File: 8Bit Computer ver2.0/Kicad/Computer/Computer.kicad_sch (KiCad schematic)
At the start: 209 parts, among them IC1 MP2338GTL-Z, IC2 MP2338GTL-Z, IC266 SN74LVC1GU04DCKR, IC267 TMUX1309DYYR, IC268 SN74LVC1G14DBVR, IC269 LM555CMX_NOPB, IC270 SN74AHC74DR, IC274 SN74AHC540DWR, IC275 SN74AHC540DWR, IC276 SN74AHC540DWR, IC277 SN74AHC540DWR, IC278 SN74AHC540DWR, IC279 SN74AHC540DWR, IC3 DS1100Z-150+, J1 M20-7910842R, J10 M20-7910842R, J11 M20-7910842R, J12 M20-7910842R, J13 M20-7910842R, J14 M20-7910842R, J15 M20-7910842R, J16 M20-7910842R, J17 M20-7910842R, J18 M20-8890845, J19 M20-8890845, J2 M20-7910842R, J20 M20-8890845, J21 M20-8890845, J22 M20-8890845, J23 M20-8890845, J24 M20-8890845, J25 M20-8890845, J26 M20-8890845, J27 M20-8890845, J28 M20-8890845, J29 M20-8890845, J3 M20-7910842R, J30 M20-8890845, J31 M20-8890845, J32 M20-8890845, J33 M20-8890845, J34 M20-8890845, J38 M20-7910842R, J39 M20-7910842R, J4 M20-7910842R, J40 M20-7911042R, J41 M20-7911042R, J5 M20-7910842R, J6 M20-7910842R, J7 M20-7910842R, J8 M20-7910842R, J9 M20-7910842R, Y1 8MHz

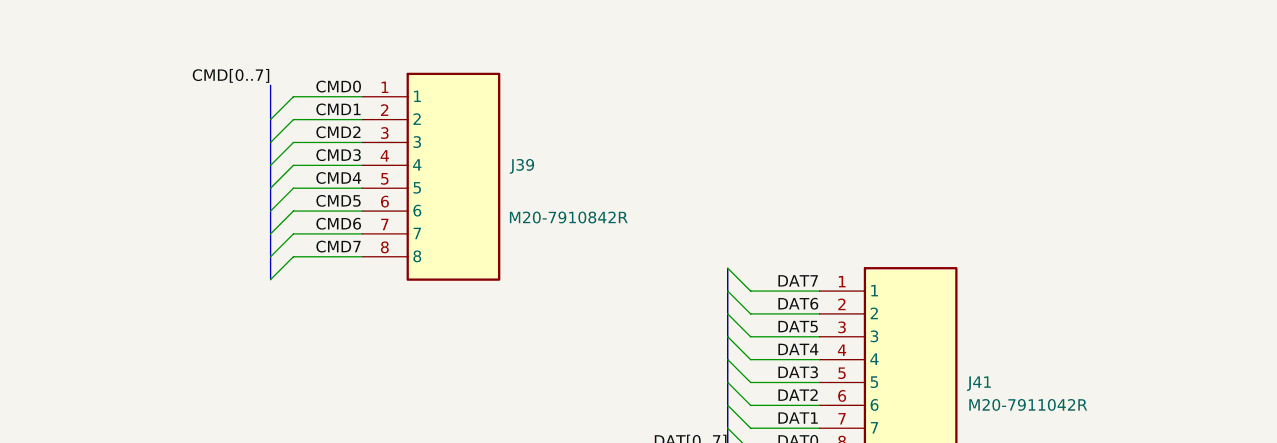
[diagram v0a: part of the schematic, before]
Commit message: Kicad
added Leds for B Bus and A Bus
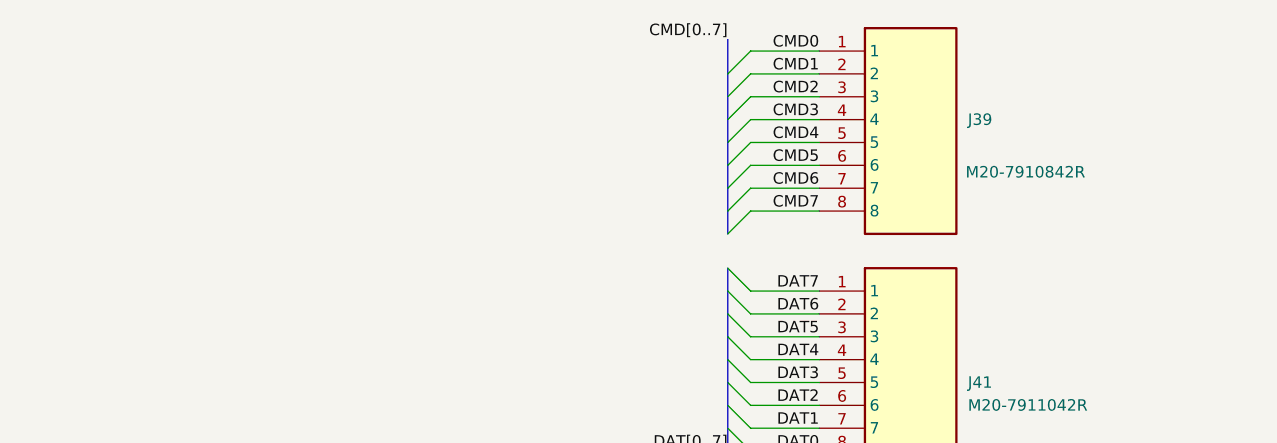
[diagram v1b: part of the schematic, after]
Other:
- moved on the sheet: J39
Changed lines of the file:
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@@
 	)
 	(bus_entry
-		(at 166.37 196.85)
+		(at 217.17 191.77)
 		(size 2.54 -2.54)
 		(stroke
@@
 	)
 	(bus_entry
-		(at 166.37 199.39)
+		(at 217.17 194.31)
 		(size 2.54 -2.54)
 		(stroke
@@
 	)
 	(bus_entry
-		(at 166.37 204.47)
+		(at 217.17 199.39)
 		(size 2.54 -2.54)
 		(stroke
@@
 	)
 	(bus_entry
-		(at 166.37 207.01)
+		(at 217.17 201.93)
 		(size 2.54 -2.54)
 		(stroke
@@
 	)
 	(bus_entry
-		(at 166.37 212.09)
+		(at 217.17 207.01)
 		(size 2.54 -2.54)
 		(stroke
@@
 	)
 	(bus_entry
-		(at 166.37 214.63)
+		(at 217.17 209.55)
 		(size 2.54 -2.54)
 		(stroke
@@
 	)
 	(bus_entry
-		(at 166.37 201.93)
+		(at 217.17 196.85)
 		(size 2.54 -2.54)
 		(stroke
@@
 	)
 	(bus_entry
-		(at 166.37 209.55)
+		(at 217.17 204.47)
 		(size 2.54 -2.54)
 		(stroke
@@
 	(bus
 		(pts
-			(xy 166.37 207.01) (xy 166.37 209.55)
+			(xy 217.17 201.93) (xy 217.17 204.47)
 		)
 		(stroke
@@
 	(bus
 		(pts
-			(xy 166.37 196.85) (xy 166.37 199.39)
+			(xy 217.17 191.77) (xy 217.17 194.31)
 		)
 		(stroke
@@
 	(wire
 		(pts
-			(xy 176.53 196.85) (xy 168.91 196.85)
+			(xy 227.33 191.77) (xy 219.71 191.77)
 		)
 		(stroke
@@
 	(bus
 		(pts
-			(xy 166.37 204.47) (xy 166.37 207.01)
+			(xy 217.17 199.39) (xy 217.17 201.93)
 		)
 		(stroke
@@
 	(bus
 		(pts
-			(xy 166.37 193.04) (xy 166.37 196.85)
+			(xy 217.17 187.96) (xy 217.17 191.77)
 		)
 		(stroke
@@
 	(wire
 		(pts
-			(xy 176.53 199.39) (xy 168.91 199.39)
+			(xy 227.33 194.31) (xy 219.71 194.31)
 		)
 		(stroke
@@
 	(bus
 		(pts
-			(xy 166.37 212.09) (xy 166.37 214.63)
+			(xy 217.17 207.01) (xy 217.17 209.55)
 		)
 		(stroke
@@
 	(wire
 		(pts
-			(xy 176.53 201.93) (xy 168.91 201.93)
+			(xy 227.33 196.85) (xy 219.71 196.85)
 		)
 		(stroke
@@
 	(wire
 		(pts
-			(xy 176.53 194.31) (xy 168.91 194.31)
+			(xy 227.33 189.23) (xy 219.71 189.23)
 		)
 		(stroke
@@
 	(bus
 		(pts
-			(xy 166.37 199.39) (xy 166.37 201.93)
+			(xy 217.17 194.31) (xy 217.17 196.85)
 		)
 		(stroke
@@
 	(wire
 		(pts
-			(xy 176.53 204.47) (xy 168.91 204.47)
+			(xy 227.33 199.39) (xy 219.71 199.39)
 		)
 		(stroke
@@
 	(bus
 		(pts
-			(xy 166.37 201.93) (xy 166.37 204.47)
+			(xy 217.17 196.85) (xy 217.17 199.39)
 		)
 		(stroke
@@
 	(wire
 		(pts
-			(xy 176.53 207.01) (xy 168.91 207.01)
+			(xy 227.33 201.93) (xy 219.71 201.93)
 		)
 		(stroke
@@
 	(wire
 		(pts
-			(xy 176.53 212.09) (xy 168.91 212.09)
+			(xy 227.33 207.01) (xy 219.71 207.01)
 		)
 		(stroke
@@
 	(wire
 		(pts
-			(xy 176.53 209.55) (xy 168.91 209.55)
+			(xy 227.33 204.47) (xy 219.71 204.47)
 		)
 		(stroke
@@
 	(bus
 		(pts
-			(xy 166.37 209.55) (xy 166.37 212.09)
+			(xy 217.17 204.47) (xy 217.17 207.01)
 		)
 		(stroke
@@
 	)
 	(label "CMD6"
-		(at 176.53 209.55 180)
+		(at 227.33 204.47 180)
 		(effects
 			(font
@@
 	)
 	(label "CMD3"
-		(at 176.53 201.93 180)
+		(at 227.33 196.85 180)
 		(effects
 			(font
@@
 	)
 	(label "CMD5"
-		(at 176.53 207.01 180)
+		(at 227.33 201.93 180)
 		(effects
 			(font
@@
 	)
 	(label "CMD2"
-		(at 176.53 199.39 180)
+		(at 227.33 194.31 180)
 		(effects
 			(font
@@
 	)
 	(label "CMD4"
-		(at 176.53 204.47 180)
+		(at 227.33 199.39 180)
 		(effects
 			(font
@@
 	)
 	(label "CMD7"
-		(at 176.53 212.09 180)
+		(at 227.33 207.01 180)
 		(effects
 			(font
@@
 	)
 	(label "CMD[0..7]"
-		(at 166.37 193.04 180)
+		(at 217.17 187.96 180)
 		(effects
 			(font
@@
 	)
 	(label "CMD0"
-		(at 176.53 194.31 180)
+		(at 227.33 189.23 180)
 		(effects
 			(font
@@
 	)
 	(label "CMD1"
-		(at 176.53 196.85 180)
+		(at 227.33 191.77 180)
 		(effects
 			(font
@@
 	(symbol
 		(lib_id "Samacsys:M20-7910842R")
-		(at 176.53 194.31 0)
+		(at 227.33 189.23 0)
 		(unit 1)
 		(exclude_from_sim no)
@@
 		(dnp no)
 		(property "Reference" "J39"
-			(at 193.04 201.9299 0)
+			(at 243.84 196.8499 0)
 			(effects
 				(font
@@
 		)
 		(property "Value" "M20-7910842R"
-			(at 192.786 207.772 0)
+			(at 243.586 202.692 0)
 			(effects
 				(font
@@
 		)
 		(property "Footprint" "Samacsys:M207910842R"
-			(at 193.04 289.23 0)
+			(at 243.84 284.15 0)
 			(effects
 				(font
@@
 		)
 		(property "Datasheet" "https://www.digikey.ph/en/products/detail/harwin-inc/M20-7910842R/6559285?msockid=39f1ec84d77b6f4428b7f904d6676eed"
-			(at 193.04 389.23 0)
+			(at 243.84 384.15 0)
 			(effects
 				(font
@@
 		)
 		(property "Description" "2.54mm (0.1\") Pitch SIL Horizontal SMT Socket Assembly, selective gold + tin (Tape & Reel packing), 8 contacts"
-			(at 176.53 194.31 0)
+			(at 227.33 189.23 0)
 			(effects
 				(font
@@
 		)
 		(property "Height" "2.65"
-			(at 193.04 589.23 0)
+			(at 243.84 584.15 0)
 			(effects
 				(font
@@
 		)
 		(property "Mouser Part Number" "855-M20-7910842R"
-			(at 193.04 689.23 0)
+			(at 243.84 684.15 0)
 			(effects
 				(font
@@
 		)
 		(property "Mouser Price/Stock" "https://www.mouser.co.uk/ProductDetail/Harwin/M20-7910842R?qs=k41KVqW3ympJ6ZCQNkwKKw%3D%3D"
-			(at 193.04 789.23 0)
+			(at 243.84 784.15 0)
 			(effects
 				(font
@@
 		)
 		(property "Manufacturer_Name" "Harwin"
-			(at 193.04 889.23 0)
+			(at 243.84 884.15 0)
 			(effects
 				(font
@@
 		)
 		(property "Manufacturer_Part_Number" "M20-7910842R"
-			(at 193.04 989.23 0)
+			(at 243.84 984.15 0)
 			(effects
 				(font

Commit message: Kicad Fixes only schematic
fixed important schematic errors
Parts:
- R112, R113, R114, R115, R116, R117, R118, R119, R120, R121, R122, R123, R124, R125, R126, R127, R128, R129, R130, R131, R132, R133, R134, R135, R136, R137, R138, R139, R140, R141, R142, R143, R144, R145, R146, R147, R148, R149, R150, R151, R152, R153, R154, R155, R156, R157, R158, R159: value 150 -> 390
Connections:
- net ADRM0: now also J27.1; no longer J27.8
- net ADRM1: now also J27.2; no longer J27.7
- net ADRM10: now also J28.3; no longer J28.6
- net ADRM11: now also J28.4; no longer J28.5
- net ADRM12: now also J28.5; no longer J28.4
- net ADRM13: now also J28.6; no longer J28.3
- net ADRM14: now also J28.7; no longer J28.2
- net ADRM15: now also J28.8; no longer J28.1
- net ADRM2: now also J27.3; no longer J27.6
- net ADRM3: now also J27.4; no longer J27.5
- net ADRM4: now also J27.5; no longer J27.4
- net ADRM5: now also J27.6; no longer J27.3
- net ADRM6: now also J27.7; no longer J27.2
- net ADRM7: now also J27.8; no longer J27.1
- net ADRM8: now also J28.1; no longer J28.8
- net ADRM9: now also J28.2; no longer J28.7
- net CMDM0: now also J29.1; no longer J29.8
- net CMDM1: now also J29.2; no longer J29.7
- net CMDM2: now also J29.3; no longer J29.6
- net CMDM3: now also J29.4; no longer J29.5
- net CMDM4: now also J29.5; no longer J29.4
- net CMDM5: now also J29.6; no longer J29.3
- net CMDM6: now also J29.7; no longer J29.2
- net CMDM7: now also J29.8; no longer J29.1
- net DATIO0: now also J33.1; no longer J33.8
- net DATIO1: now also J33.2; no longer J33.7
- net DATIO2: now also J33.3; no longer J33.6
- net DATIO3: now also J33.4; no longer J33.5
- net DATIO4: now also J33.5; no longer J33.4
- net DATIO5: now also J33.6; no longer J33.3
- net DATIO6: now also J33.7; no longer J33.2
- net DATIO7: now also J33.8; no longer J33.1
- net DATM0: now also J30.1; no longer J30.8
- net DATM1: now also J30.2; no longer J30.7
- net DATM2: now also J30.3; no longer J30.6
- net DATM3: now also J30.4; no longer J30.5
- net DATM4: now also J30.5; no longer J30.4
- net DATM5: now also J30.6; no longer J30.3
- net DATM6: now also J30.7; no longer J30.2
- net DATM7: now also J30.8; no longer J30.1
- net GND: now also J14.1, J14.2; no longer J14.7, J14.8
- net LDADR_{dis}: now also J14.6; no longer J14.3
- net LNM0: now also J25.1; no longer J25.8
- net LNM1: now also J25.2; no longer J25.7
- net LNM10: now also J26.3; no longer J26.6
- net LNM11: now also J26.4; no longer J26.5
- net LNM12: now also J26.5; no longer J26.4
- net LNM13: now also J26.6; no longer J26.3
- net LNM14: now also J26.7; no longer J26.2
- net LNM15: now also J26.8; no longer J26.1
- net LNM2: now also J25.3; no longer J25.6
- net LNM3: now also J25.4; no longer J25.5
- net LNM4: now also J25.5; no longer J25.4
- net LNM5: now also J25.6; no longer J25.3
- net LNM6: now also J25.7; no longer J25.2
- net LNM7: now also J25.8; no longer J25.1
- net LNM8: now also J26.1; no longer J26.8
- net LNM9: now also J26.2; no longer J26.7
- net VBUS: now also J14.3, J14.4; no longer J14.5, J14.6
- net ~{CLKd}: now also J14.8; no longer J14.1
- net ~{CLK}: now also J14.7; no longer J14.2
- net at D27.1 (K), J17.8: now also J14.5; no longer J14.4
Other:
- moved on the sheet: J25, J26, J27, J28, J29, J30, J33

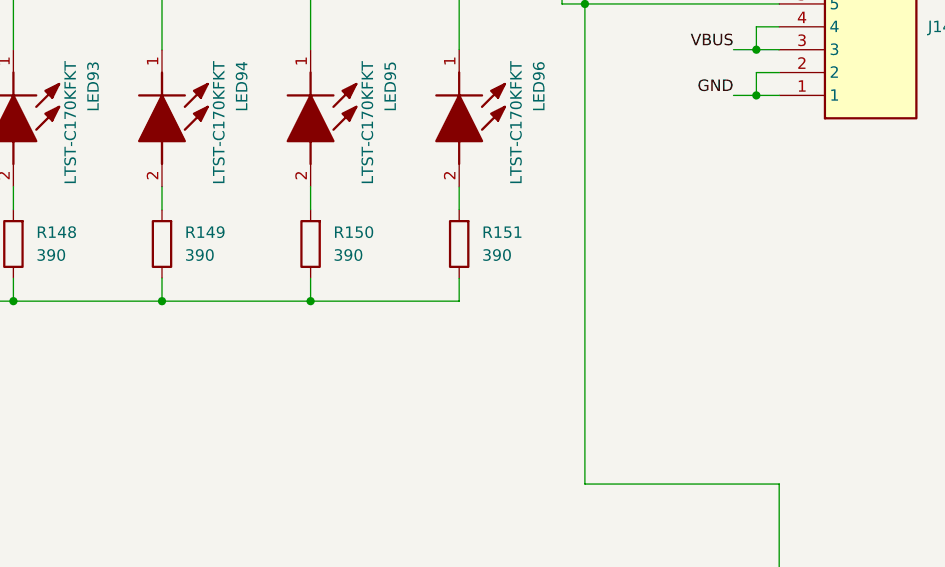
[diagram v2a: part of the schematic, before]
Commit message: Kicad, PCB Fix
fixed the errors on the PCB
added mounting holes
added GND panels on Top and Bot Layer
added 100uF
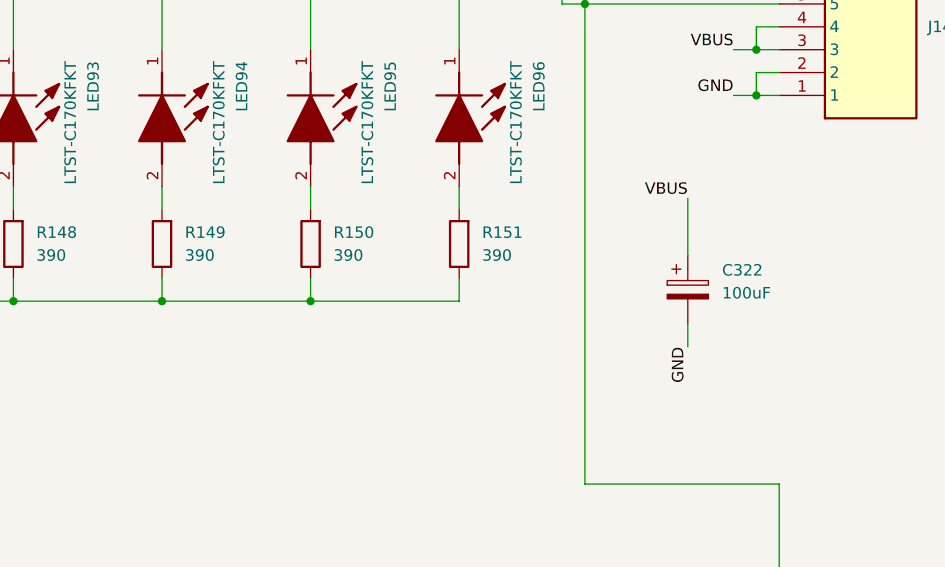
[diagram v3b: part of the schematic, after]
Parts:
- added C322: 100uF, Capacitor_THT:CP_Radial_D8.0mm_P3.50mm, symbol Device:C_Polarized
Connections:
- net GND: now also C322.2
- net VBUS: now also C322.1
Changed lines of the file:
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@@
 	(wire
 		(pts
+			(xy 217.17 694.69) (xy 217.17 697.23)
+		)
+		(stroke
+			(width 0)
+			(type default)
+		)
+	)
+	(wire
+		(pts
 			(xy 162.56 612.14) (xy 187.96 612.14)
 		)
@@
 	(wire
 		(pts
-			(xy 175.26 692.15) (xy 158.75 692.15)
+			(xy 158.75 692.15) (xy 175.26 692.15)
 		)
 		(stroke
@@
 	(wire
 		(pts
+			(xy 217.17 680.72) (xy 217.17 687.07)
+		)
+		(stroke
+			(width 0)
+			(type default)
+		)
+	)
+	(wire
+		(pts
 			(xy 36.83 389.89) (xy 39.37 389.89)
 		)
@@
 		)
 	)
+	(label "GND"
+		(at 217.17 697.23 270)
+		(effects
+			(font
+				(size 1.27 1.27)
+			)
+			(justify right bottom)
+		)
+	)
 	(label "CMDM7"
 		(at 358.14 646.43 0)
@@
 		)
 	)
+	(label "VBUS"
+		(at 217.17 680.72 180)
+		(effects
+			(font
+				(size 1.27 1.27)
+			)
+			(justify right bottom)
+		)
+	)
 	(label "GND"
 		(at 69.85 454.66 0)
@@
 		(length 2.54)
 		(shape round)
-		(at 345.44 786.13 0)
+		(at 344.17 791.21 0)
 		(fields_autoplaced yes)
 		(effects
@@
 		)
 		(property "Netclass" "CLK"
-			(at 346.1385 783.59 0)
+			(at 344.8685 788.67 0)
 			(effects
 				(font
@@
 		)
 		(property "Component Class" ""
-			(at -172.72 372.11 0)
+			(at -173.99 377.19 0)
 			(effects
 				(font
@@
 					(unit 1)
 				)
+			)
+		)
+	)
+	(symbol
+		(lib_id "Device:C_Polarized")
+		(at 217.17 690.88 0)
+		(unit 1)
+		(exclude_from_sim no)
+		(in_bom yes)
+		(on_board yes)
+		(dnp no)
+		(fields_autoplaced yes)
+		(property "Reference" "C322"
+			(at 220.98 688.7209 0)
+			(effects
+				(font
+					(size 1.27 1.27)
+				)
+				(justify left)
+			)
+		)
+		(property "Value" "100uF"
+			(at 220.98 691.2609 0)
+			(effects
+				(font
+					(size 1.27 1.27)
+				)
+				(justify left)
+			)
+		)
+		(property "Footprint" "Capacitor_THT:CP_Radial_D8.0mm_P3.50mm"
+			(at 218.1352 694.69 0)
+			(effects
+				(font
+					(size 1.27 1.27)
+				)
+				(hide yes)
+			)
+		)
+		(property "Datasheet" "~"
+			(at 217.17 690.88 0)
+			(effects
+				(font
+					(size 1.27 1.27)
+				)
+				(hide yes)
+			)
+		)
+		(property "Description" "Polarized capacitor"
+			(at 217.17 690.88 0)
+			(effects
+				(font
+					(size 1.27 1.27)
+				)
+				(hide yes)
+			)
+		)
+		(pin "2"
+		)
+		(pin "1"
+		)
+		(instances
+			(project "Computer"
+				(path "/1196a00e-6878-4d6d-82b7-9e052dfe7c14"
+					(reference "C322")
+					(unit 1)
+				)

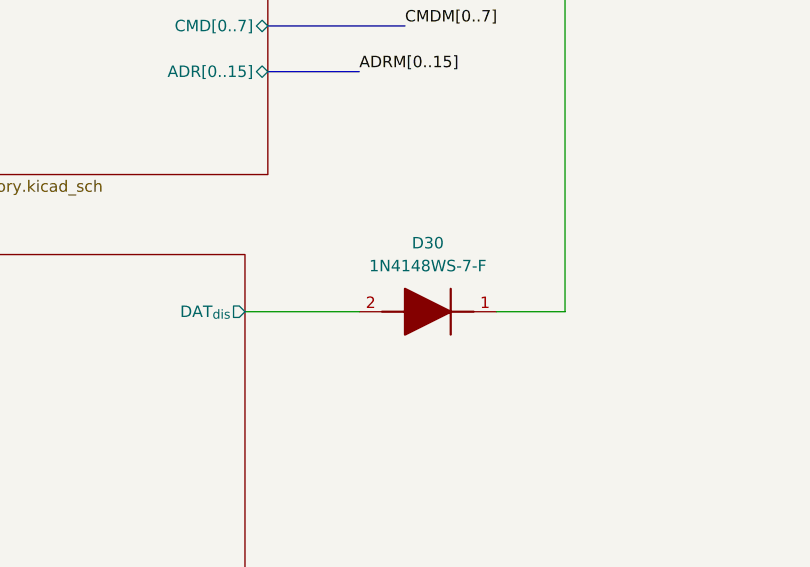
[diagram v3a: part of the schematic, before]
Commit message: updated T76 software, Kicad bugs
changed the inverting outs of IC199 to non inverting
changed Pin of CMD decoder IC237 0x2A from GND to VCC (pin5)
deleted diode d30
changed silkscreen of the Clock gen mux from 0 1 555 to 1 0 555 and buttonclk from 1 0 to 0 1
changed the DS1100-150+ of the edge detector to an or gate SN74HCS32
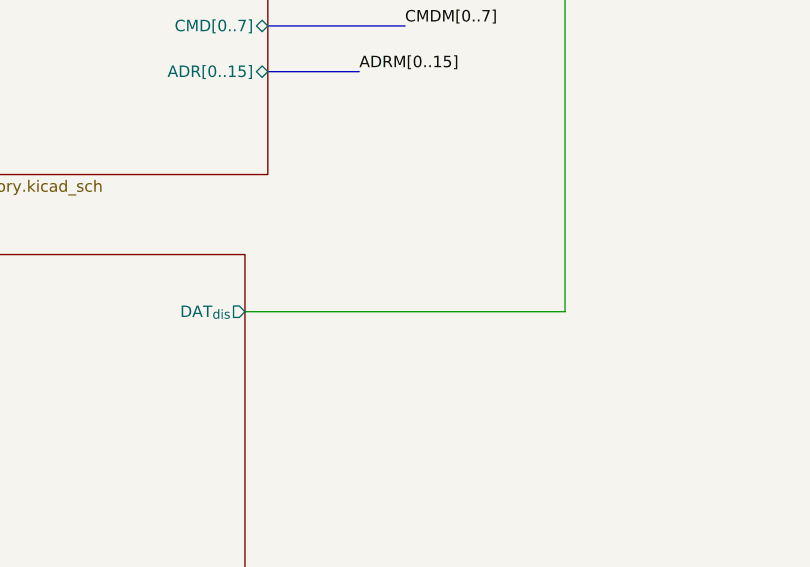
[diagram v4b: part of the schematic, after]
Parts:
- removed D30: 1N4148WS-7-F, Samacsys:SOD2513X120N, symbol Samacsys:1N4148WS-7-F
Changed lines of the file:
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@@
 	(wire
 		(pts
-			(xy 520.7 650.24) (xy 528.32 650.24)
-		)
-		(stroke
-			(width 0)
-			(type default)
-		)
-	)
-	(wire
-		(pts
 			(xy 77.47 774.7) (xy 77.47 777.24)
 		)
@@
 	(wire
 		(pts
-			(xy 492.76 650.24) (xy 505.46 650.24)
+			(xy 492.76 650.24) (xy 528.32 650.24)
 		)
 		(stroke
@@
 					(unit 1)
 				)
-			)
-		)
-	)
-	(symbol
-		(lib_id "Samacsys:1N4148WS-7-F")
-		(at 520.7 650.24 180)
-		(unit 1)
-		(exclude_from_sim no)
-		(in_bom yes)
-		(on_board yes)
-		(dnp no)
-		(fields_autoplaced yes)
-		(property "Reference" "D30"
-			(at 513.08 642.62 0)
-			(effects
-				(font
-					(size 1.27 1.27)
-				)
-			)
-		)
-		(property "Value" "1N4148WS-7-F"
-			(at 513.08 645.16 0)
-			(effects
-				(font
-					(size 1.27 1.27)
-				)
-			)
-		)
-		(property "Footprint" "Samacsys:SOD2513X120N"
-			(at 509.27 552.78 0)
-			(effects
-				(font
-					(size 1.27 1.27)
-				)
-				(justify left top)
-				(hide yes)
-			)
-		)
-		(property "Datasheet" "https://www.diodes.com//assets/Datasheets/1N4148WS_BAV16WS.pdf"
-			(at 509.27 452.78 0)
-			(effects
-				(font
-					(size 1.27 1.27)
-				)
-				(justify left top)
-				(hide yes)
-			)
-		)
-		(property "Description" "Diode Switching 150mA 75V 200mW SOD323 Diodes Inc 1N4148WS-7-F Switching Diode, 150mA 75V, 2-Pin SOD-323"
-			(at 520.7 650.24 0)
-			(effects
-				(font
-					(size 1.27 1.27)
-				)
-				(hide yes)
-			)
-		)
-		(property "Height" "1.2"
-			(at 509.27 252.78 0)
-			(effects
-				(font
-					(size 1.27 1.27)
-				)
-				(justify left top)
-				(hide yes)
-			)
-		)
-		(property "Mouser Part Number" "621-1N4148WS-F"
-			(at 509.27 152.78 0)
-			(effects
-				(font
-					(size 1.27 1.27)
-				)
-				(justify left top)
-				(hide yes)
-			)
-		)
-		(property "Mouser Price/Stock" "https://www.mouser.co.uk/ProductDetail/Diodes-Incorporated/1N4148WS-7-F?qs=4drIV0IxA0r8aNy7%2Fu4kVw%3D%3D"
-			(at 509.27 52.78 0)
-			(effects
-				(font
-					(size 1.27 1.27)
-				)
-				(justify left top)
-				(hide yes)
-			)
-		)
-		(property "Manufacturer_Name" "Diodes Incorporated"
-			(at 509.27 -47.22 0)
-			(effects
-				(font
-					(size 1.27 1.27)
-				)
-				(justify left top)
-				(hide yes)
-			)
-		)
-		(property "Manufacturer_Part_Number" "1N4148WS-7-F"
-			(at 509.27 -147.22 0)
-			(effects
-				(font
-					(size 1.27 1.27)
-				)
-				(justify left top)
-				(hide yes)
-			)
-		)
-		(pin "1"
-		)
-		(pin "2"
-		)
-		(instances
-			(project ""
-				(path "/1196a00e-6878-4d6d-82b7-9e052dfe7c14"
-					(reference "D30")
-					(unit 1)
-				)
